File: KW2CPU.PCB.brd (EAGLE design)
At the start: 50 x 30 mm, 71 parts, among them J1 DF12_M, J2 MOLEX55560-0207, J3 MMCX_VERT, U1 MKW21D, U2 AT45DB161D8S1, U3 RF6555, U5 F-ANTENNA, X1 32KHZ, X2 32MHZ

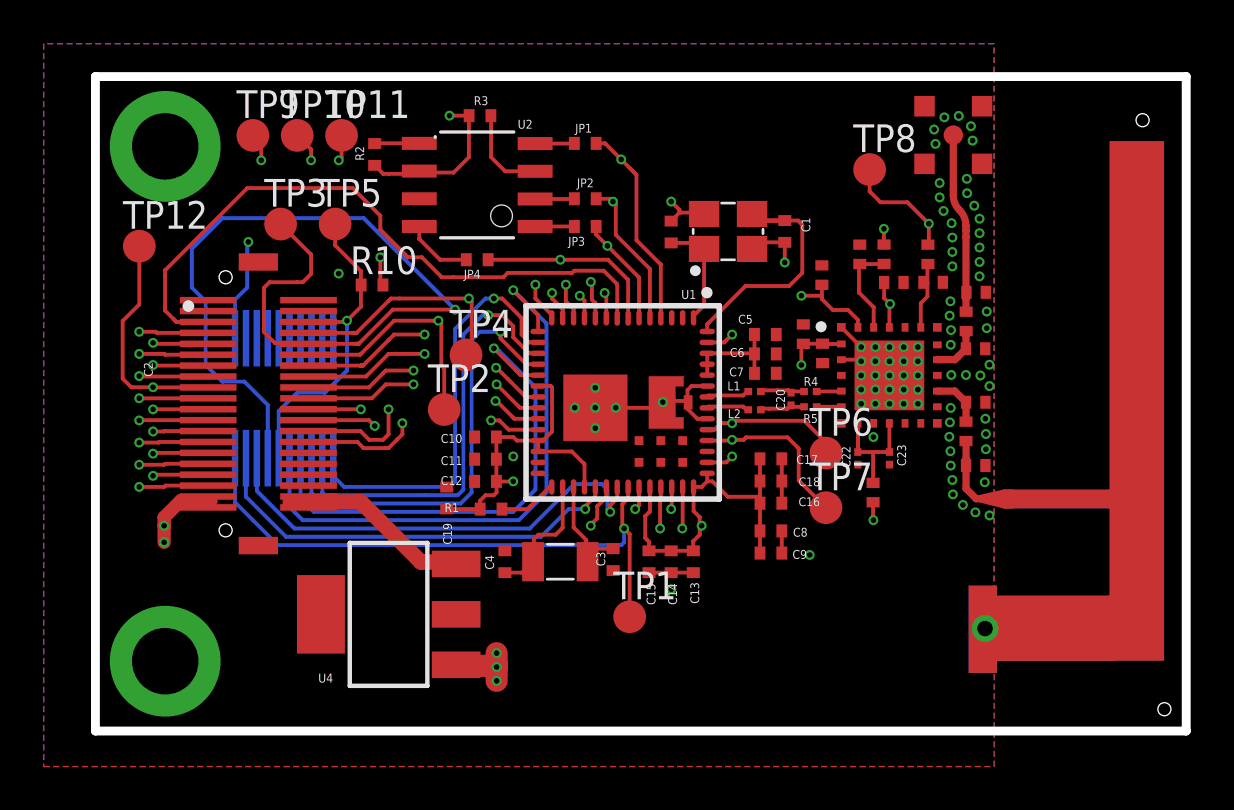
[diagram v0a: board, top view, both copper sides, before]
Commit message: Switched Flash for EEPROM
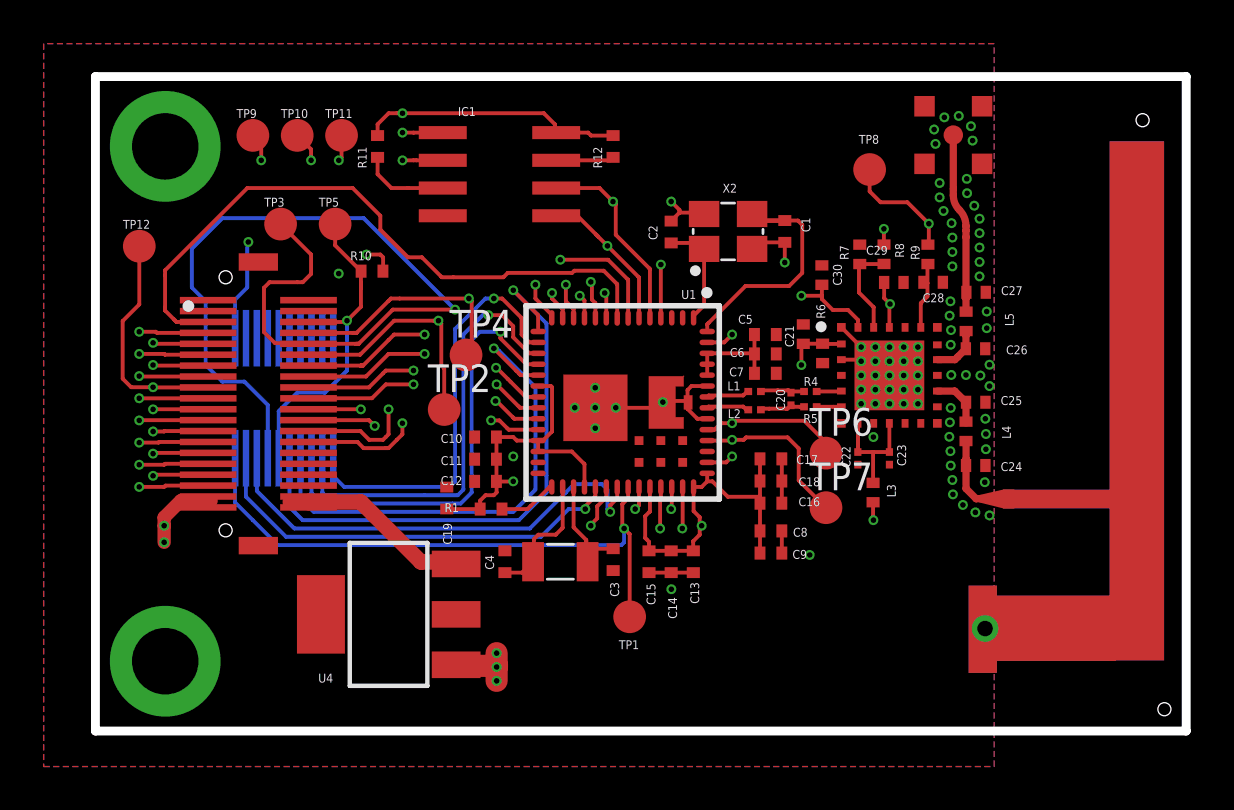
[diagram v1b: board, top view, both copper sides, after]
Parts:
- removed JP1, JP2, JP3, JP4: (no value), GW-devices:RF-R0402
- removed R2, R3: 10k, GW-devices:RF-R0402
- removed U2: AT45DB161D8S1, KW2:8S1
- added IC1: 25AA080SN, microchip:SO-08
- added R11, R12: 10k, GW-devices:RF-R0402
- moved R10 0.63 mm to (4.19, 5.84)
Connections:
- removed net !CS: JP1.1, U2.4
- removed net N$54: JP4.1, U2.8
- removed net N$8: R3.1, U2.3
- removed net N$9: R2.1, U2.5
- removed net SCK: JP2.1, U2.2
- removed net SI: JP3.1, U2.1
- new net N$1: IC1.3, R11.1
- new net N$2: IC1.7, R12.1
- net +3V3: now also IC1.8, R11.2, R12.2; no longer R2.2, R3.2, U2.6
- net GND: now also IC1.4; no longer U2.7
- net PTC4/LLWU_P8/SPI0_PCS0/UART1_TX/FTM0_CH3/CMP1_OUT: no longer JP1.2
- net PTC5/LLWU_P8/SPI0_PCS0/UART1_TX/FTM0_CH3/CMP1_OUT: now also IC1.6; no longer JP2.2
- net PTC6/LLWU_P10/CMP0_IN0/SPI0_SOUT/PDB0_EXTRG/I2S0_RX_BCLK/I2S0_MCLK: now also IC1.5; no longer JP3.2
- net PTC7/CMP0_IN1/SPI0_SIN/USB_SOF_OUT/I2S0_RX_FS: now also IC1.2; no longer JP4.2
- net PTD5/ADC0_SE6B/SPI0_PCS2/!UART0_CTS!/!UART0_COL!/FTM0_CH5/!EWM_OUT: now also IC1.1
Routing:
- net PTC7/CMP0_IN1/SPI0_SIN/USB_SOF_OUT/I2S0_RX_FS: track 26.8 -> 43.5 mm, vias 2 -> 3
- net PTD5/ADC0_SE6B/SPI0_PCS2/!UART0_CTS!/!UART0_COL!/FTM0_CH5/!EWM_OUT: track 51.7 -> 58.4 mm, vias 3 -> 4
- net +3V3: track 59.1 -> 63.7 mm
- net N$1: track 0.00 -> 4.27 mm
- net N$8: track 4.19 -> 0.00 mm
- net N$54: track 3.13 -> 0.00 mm
- net N$2: track 0.00 -> 2.66 mm
- net PTC4/LLWU_P8/SPI0_PCS0/UART1_TX/FTM0_CH3/CMP1_OUT: track 34.1 -> 36.5 mm
- net PTC5/LLWU_P8/SPI0_PCS0/UART1_TX/FTM0_CH3/CMP1_OUT: track 28.7 -> 30.9 mm
- net N$9: track 2.05 -> 0.00 mm
- net PTC6/LLWU_P10/CMP0_IN0/SPI0_SOUT/PDB0_EXTRG/I2S0_RX_BCLK/I2S0_MCLK: track 25.7 -> 27.6 mm
- net SCK: track 1.80 -> 0.00 mm
- net !CS: track 1.80 -> 0.00 mm
- net SI: track 1.80 -> 0.00 mm
